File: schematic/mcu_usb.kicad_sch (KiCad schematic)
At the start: 40 parts, among them J2 USB4105-xx-A, J3 TC2030-IDC-NL, U1 STM32H563ZIT6, U4 USBLC6-2SC6, U5 TMP1075D, Y1 25MHz ABM8G

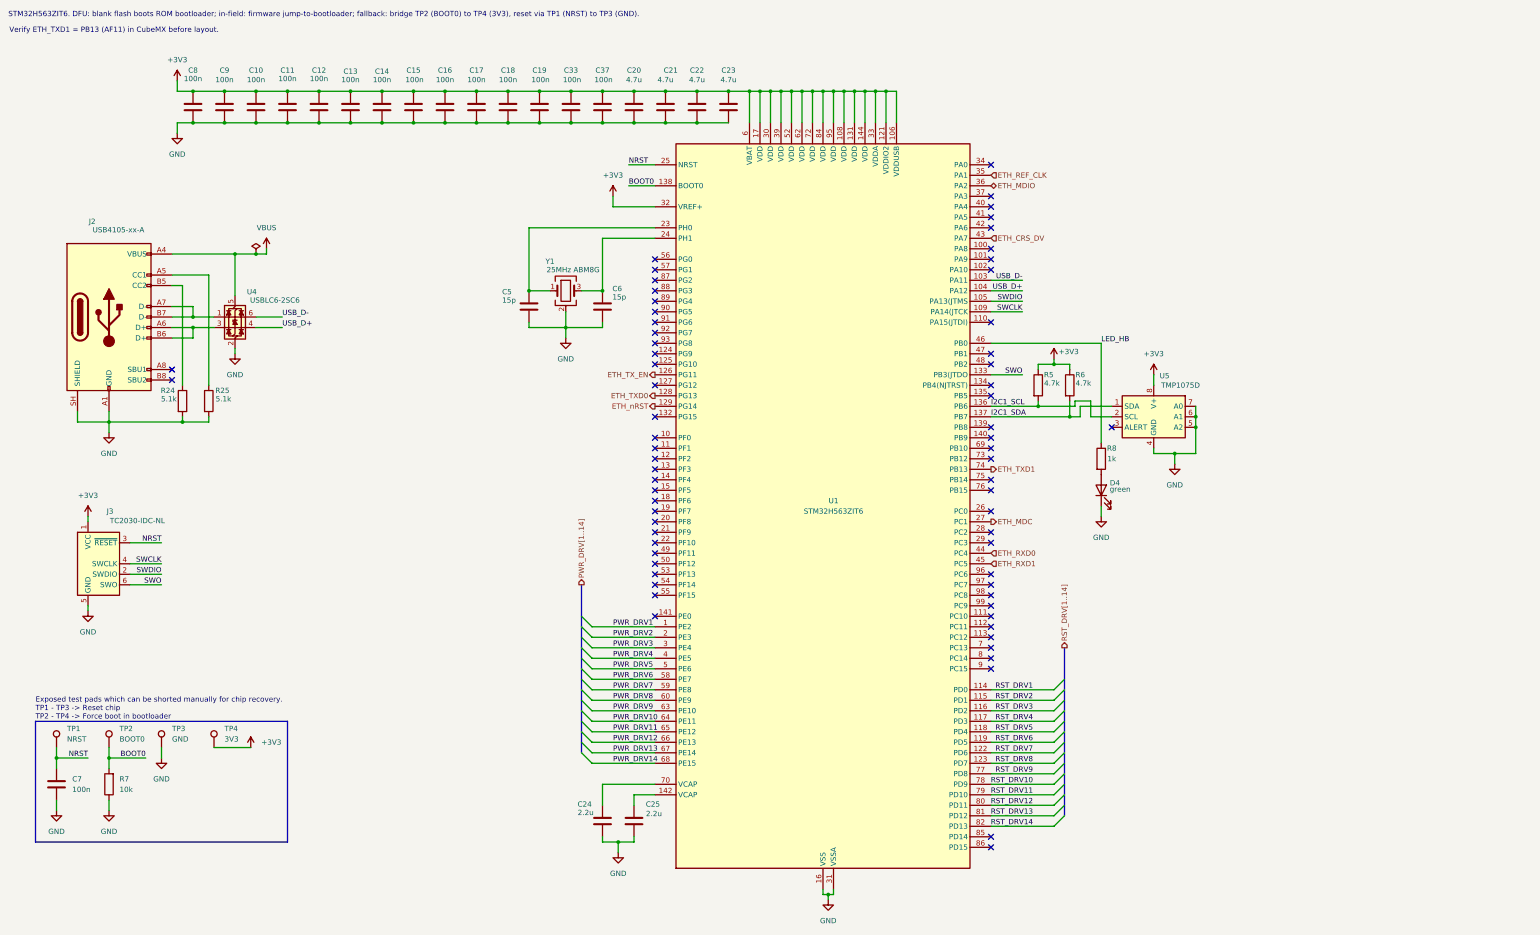
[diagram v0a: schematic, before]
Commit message: Swap to smaller MCU package with less pins
Signed-off-by: Lee Smet <lee.smet@hotmail.com>
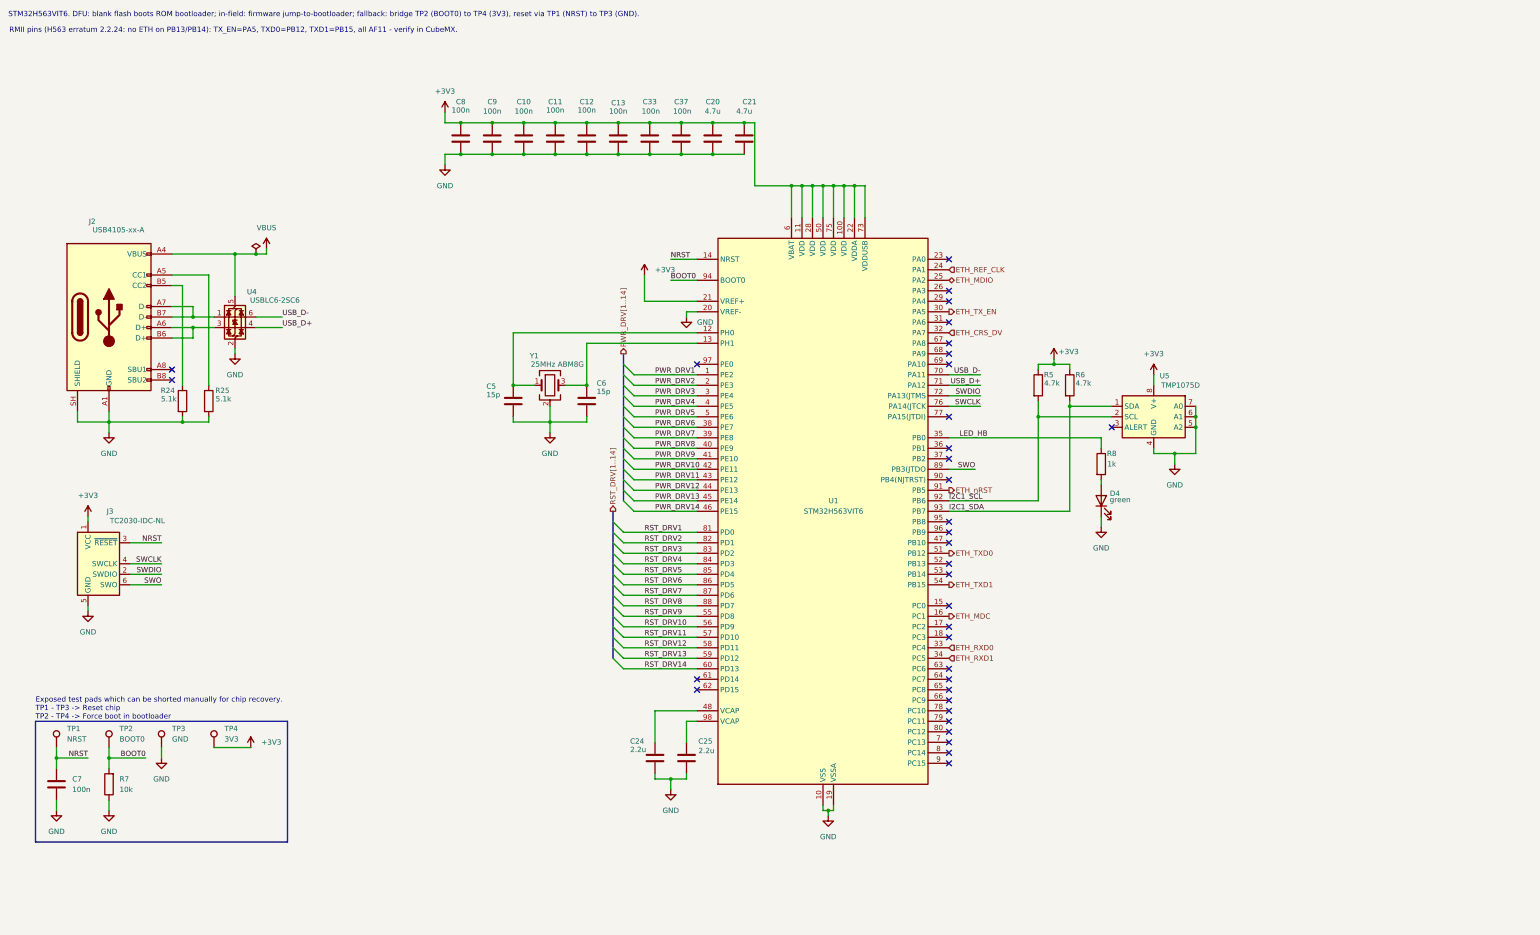
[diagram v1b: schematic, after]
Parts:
- removed C14, C15, C16, C17, C18, C19: 100n, Capacitor_SMD:C_0402_1005Metric, symbol Device:C
- removed C22, C23: 4.7u, Capacitor_SMD:C_0603_1608Metric, symbol Device:C
- U1: value STM32H563ZIT6 -> STM32H563VIT6; footprint Package_QFP:LQFP-144_20x20mm_P0.5mm -> Package_QFP:LQFP-100_14x14mm_P0.5mm; symbol MCU_ST_STM32H5:STM32H563ZITx -> MCU_ST_STM32H5:STM32H563VITx
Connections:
- net +3V3: now also U1.100 (VDD), U1.11 (VDD), U1.21 (VREF+), U1.22 (VDDA), U1.28 (VDD), U1.50 (VDD), U1.73 (VDDUSB), U1.75 (VDD); no longer U1.106 (VDDUSB), U1.108 (VDD), U1.121 (VDDIO2), U1.131 (VDD), U1.144 (VDD), U1.17 (VDD), U1.30 (VDD), U1.32 (VREF+), U1.33 (VDDA), U1.39 (VDD), U1.52 (VDD), U1.62 (VDD), U1.72 (VDD), U1.84 (VDD), U1.95 (VDD)
- net BOOT0: now also U1.94 (BOOT0); no longer U1.138 (BOOT0)
- net ETH_CRS_DV: now also U1.32 (PA7); no longer U1.43 (PA7)
- net ETH_MDC: now also U1.16 (PC1); no longer U1.27 (PC1)
- net ETH_MDIO: now also U1.25 (PA2); no longer U1.36 (PA2)
- net ETH_REF_CLK: now also U1.24 (PA1); no longer U1.35 (PA1)
- net ETH_RXD0: now also U1.33 (PC4); no longer U1.44 (PC4)
- net ETH_RXD1: now also U1.34 (PC5); no longer U1.45 (PC5)
- net ETH_TXD0: now also U1.51 (PB12); no longer U1.128 (PG13)
- net ETH_TXD1: now also U1.54 (PB15); no longer U1.74 (PB13)
- net ETH_TX_EN: now also U1.30 (PA5); no longer U1.126 (PG11)
- net ETH_nRST: now also U1.91 (PB5); no longer U1.129 (PG14)
- net GND: now also U1.10 (VSS), U1.19 (VSSA), U1.20 (VREF-), U1.27 (VSS), U1.49 (VSS), U1.74 (VSS), U1.99 (VSS); no longer U1.107 (VSS), U1.120 (VSS), U1.130 (VSS), U1.143 (VSS), U1.16 (VSS), U1.31 (VSSA), U1.38 (VSS), U1.51 (VSS), U1.61 (VSS), U1.71 (VSS), U1.83 (VSS), U1.94 (VSS)
- net I2C1_SCL: now also U1.92 (PB6); no longer U1.136 (PB6)
- net I2C1_SDA: now also U1.93 (PB7); no longer U1.137 (PB7)
- net LED_HB: now also U1.35 (PB0); no longer U1.46 (PB0)
- net NRST: now also U1.14 (NRST); no longer U1.25 (NRST)
- net PWR_DRV10: now also U1.42 (PE11); no longer U1.64 (PE11)
- net PWR_DRV11: now also U1.43 (PE12); no longer U1.65 (PE12)
- net PWR_DRV12: now also U1.44 (PE13); no longer U1.66 (PE13)
- net PWR_DRV13: now also U1.45 (PE14); no longer U1.67 (PE14)
- net PWR_DRV14: now also U1.46 (PE15); no longer U1.68 (PE15)
- net PWR_DRV6: now also U1.38 (PE7); no longer U1.58 (PE7)
- net PWR_DRV7: now also U1.39 (PE8); no longer U1.59 (PE8)
- net PWR_DRV8: now also U1.40 (PE9); no longer U1.60 (PE9)
- net PWR_DRV9: now also U1.41 (PE10); no longer U1.63 (PE10)
- net RST_DRV1: now also U1.81 (PD0); no longer U1.114 (PD0)
- net RST_DRV10: now also U1.56 (PD9); no longer U1.78 (PD9)
- net RST_DRV11: now also U1.57 (PD10); no longer U1.79 (PD10)
- net RST_DRV12: now also U1.58 (PD11); no longer U1.80 (PD11)
- net RST_DRV13: now also U1.59 (PD12); no longer U1.81 (PD12)
- net RST_DRV14: now also U1.60 (PD13); no longer U1.82 (PD13)
- net RST_DRV2: now also U1.82 (PD1); no longer U1.115 (PD1)
- net RST_DRV3: now also U1.83 (PD2); no longer U1.116 (PD2)
- net RST_DRV4: now also U1.84 (PD3); no longer U1.117 (PD3)
- net RST_DRV5: now also U1.85 (PD4); no longer U1.118 (PD4)
- net RST_DRV6: now also U1.86 (PD5); no longer U1.119 (PD5)
- net RST_DRV7: now also U1.87 (PD6); no longer U1.122 (PD6)
- net RST_DRV8: now also U1.88 (PD7); no longer U1.123 (PD7)
- net RST_DRV9: now also U1.55 (PD8); no longer U1.77 (PD8)
- net SWCLK: now also U1.76 (PA14(JTCK); no longer U1.109 (PA14(JTCK)
- net SWDIO: now also U1.72 (PA13(JTMS); no longer U1.105 (PA13(JTMS)
- net SWO: now also U1.89 (PB3(JTDO); no longer U1.133 (PB3(JTDO)
- net USB_D+: now also U1.71 (PA12); no longer U1.104 (PA12)
- net USB_D-: now also U1.70 (PA11); no longer U1.103 (PA11)
- net at C6.1, Y1.3: now also U1.13 (PH1); no longer U1.24 (PH1)
- net at U1.12 (PH0): now also C5.1, Y1.1
- net at C25.1: now also U1.98 (VCAP); no longer U1.142 (VCAP)
- net at U1.48 (VCAP): now also C24.1
- now unconnected: U1.23 (PH0)
- no-connect marks 67 -> 35
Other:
- note added: "RMII pins (H563 erratum 2.2.24: no ETH on PB13/PB14): TX_EN=PA5, TXD0=PB12, TXD1=PB15, all AF11 - verify in CubeMX."
- note added: "STM32H563VIT6. DFU: blank flash boots ROM bootloader; in-field: firmware jump-to-bootloader; fallback: bridge TP2 (BOOT0) to TP4 (3V3), reset via TP1 (NRST) to TP3 (GND)."
- note removed: "STM32H563ZIT6. DFU: blank flash boots ROM bootloader; in-field: firmware jump-to-bootloader; fallback: bridge TP2 (BOOT0) to TP4 (3V3), reset via TP1 (NRST) to TP3 (GND)."
- note removed: "Verify ETH_TXD1 = PB13 (AF11) in CubeMX before layout."
- moved on the sheet: C10, C11, C12, C13, C20, C21, C24, C25, C33, C37, C5, C6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

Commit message: More schematic works
Signed-off-by: Lee Smet <lee.smet@hotmail.com>
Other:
- note added: "One 100nF cap per supply pin Bulk caps: 1 on power trace entry in MCU area, 1 on other side of MCU, relaxed"
- moved on the sheet: C10, C11, C12, C13, C20, C21, C33, C37, C8, C9

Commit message: Add manufacturer and MPN to schematic parts
Signed-off-by: Lee Smet <lee.smet@hotmail.com>
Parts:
- C10, C11, C12, C13, C33, C37, C7, C8, C9: MANUFACTURER (none) -> YAGEO; MPN (none) -> CC0402KRX7R7BB104
- C20, C21: MANUFACTURER (none) -> Samsung Electro-Mechanics; MPN (none) -> CL10A475KO8NNNC
- C24, C25: MANUFACTURER (none) -> Samsung Electro-Mechanics; MPN (none) -> CL10A225KA8NNNC
- C5, C6: MANUFACTURER (none) -> Murata; MPN (none) -> GRM1555C1H150JA01D
- D4: MANUFACTURER (none) -> Kingbright; MPN (none) -> APT1608LZGCK
- J2: MANUFACTURER (none) -> Global Connector Technology; MPN (none) -> USB4105-GF-A
- J3: MANUFACTURER (none) -> Tag-Connect; MPN (none) -> TC2030-IDC-NL
- R24, R25: MANUFACTURER (none) -> YAGEO; MPN (none) -> RC0402FR-075K1L
- R5, R6: MANUFACTURER (none) -> YAGEO; MPN (none) -> RC0402FR-074K7L
- R7: MANUFACTURER (none) -> UNI-ROYAL; MPN (none) -> 0402WGF1002TCE
- R8: MANUFACTURER (none) -> YAGEO; MPN (none) -> RC0402FR-071KL
- U1: MANUFACTURER (none) -> STMicroelectronics; MPN (none) -> STM32H563VIT6
- U4: MANUFACTURER (none) -> STMicroelectronics; MPN (none) -> USBLC6-2SC6
- U5: MANUFACTURER (none) -> Texas Instruments; MPN (none) -> TMP1075DR
- Y1: MANUFACTURER (none) -> Abracon; MPN (none) -> ABM8G-25.000MHZ-B4Y-T3

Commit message: Finish adding external temp probes
Signed-off-by: Lee Smet <lee.smet@hotmail.com>
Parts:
- added D5: ESD9L5.0ST5G, Diode_SMD:D_SOD-923, symbol Device:D_Zener
- added J4, J5, J6, J7: 1WIRE, Connector_JST:JST_PH_B3B-PH-K_1x03_P2.00mm_Vertical, symbol Connector_Generic:Conn_01x03
- added R30: 4.7k, Resistor_SMD:R_0402_1005Metric, symbol Device:R
- added R31: 100, Resistor_SMD:R_0603_1608Metric, symbol Device:R
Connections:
- net +3V3: now also J4.1 (Pin_1), J5.1 (Pin_1), J6.1 (Pin_1), J7.1 (Pin_1), R30.1
- net GND: now also D5.2 (A), J4.3 (Pin_3), J5.3 (Pin_3), J6.3 (Pin_3), J7.3 (Pin_3)
- net OW_MCU: now reaches U1.68 (PA9)
- net OW_MCU: now also R31.1
- new net OW_DATA: D5.1 (K), J4.2 (Pin_2), J5.2 (Pin_2), J6.2 (Pin_2), J7.2 (Pin_2), R30.2, R31.2
- no-connect marks 35 -> 34
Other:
- note added: "External Temperature Probe Connectors Connect to DS18B20 temperature probes"

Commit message: Exclude test pads and Tag-Connect land from BOM
TP1-TP4 and J3 are bare copper with nothing to place; keep them out
of the assembly BOM. Footprint attributes updated to match.
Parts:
- J3, TP1, TP2, TP3, TP4: now left out of the parts list

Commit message: Add protected GPIO expansion header
New sheet 'Expansion header' with J8, a 2x18 2.54 mm header (DNP),
bringing out the 28 spare U1 GPIOs plus I2C1, 3V3 and 5V.

- Each signal: 330R series resistor (4x0402 array, MCU side) and a
  TPD4E05U06 ESD clamp at the header pin.
- 3V3 and 5V header pins: PTC fuse plus a TVS to GND.
- PC13-PC15 stay unconnected (backup domain, LSE).
- U1 spare pins labelled GPIO_<pin>; the I2C1 labels on U1 became
  global so the header can reach the bus. Net class patterns added
  for I2C1_*, HDR_3V3 and HDR_5V.
- Board regenerated from the netlist (nothing was placed yet).
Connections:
- net GPIO_PC0: now reaches U1.15 (PC0)
- net GPIO_PC2: now reaches U1.17 (PC2)
- net GPIO_PC3: now reaches U1.18 (PC3)
- net GPIO_PA0: now reaches U1.23 (PA0)
- net GPIO_PA3: now reaches U1.26 (PA3)
- net GPIO_PA4: now reaches U1.29 (PA4)
- net GPIO_PA6: now reaches U1.31 (PA6)
- net GPIO_PB1: now reaches U1.36 (PB1)
- net GPIO_PB2: now reaches U1.37 (PB2)
- net GPIO_PB10: now reaches U1.47 (PB10)
- net GPIO_PB13: now reaches U1.52 (PB13)
- net GPIO_PB14: now reaches U1.53 (PB14)
- net GPIO_PD14: now reaches U1.61 (PD14)
- net GPIO_PD15: now reaches U1.62 (PD15)
- net GPIO_PC6: now reaches U1.63 (PC6)
- net GPIO_PC7: now reaches U1.64 (PC7)
- net GPIO_PC8: now reaches U1.65 (PC8)
- net GPIO_PC9: now reaches U1.66 (PC9)
- net GPIO_PA8: now reaches U1.67 (PA8)
- net GPIO_PA10: now reaches U1.69 (PA10)
- net GPIO_PA15: now reaches U1.77 (PA15(JTDI))
- net GPIO_PC10: now reaches U1.78 (PC10)
- net GPIO_PC11: now reaches U1.79 (PC11)
- net GPIO_PC12: now reaches U1.80 (PC12)
- net GPIO_PB4: now reaches U1.90 (PB4(NJTRST))
- net GPIO_PB8: now reaches U1.95 (PB8)
- net GPIO_PB9: now reaches U1.96 (PB9)
- net GPIO_PE0: now reaches U1.97 (PE0)
- no-connect marks 34 -> 6

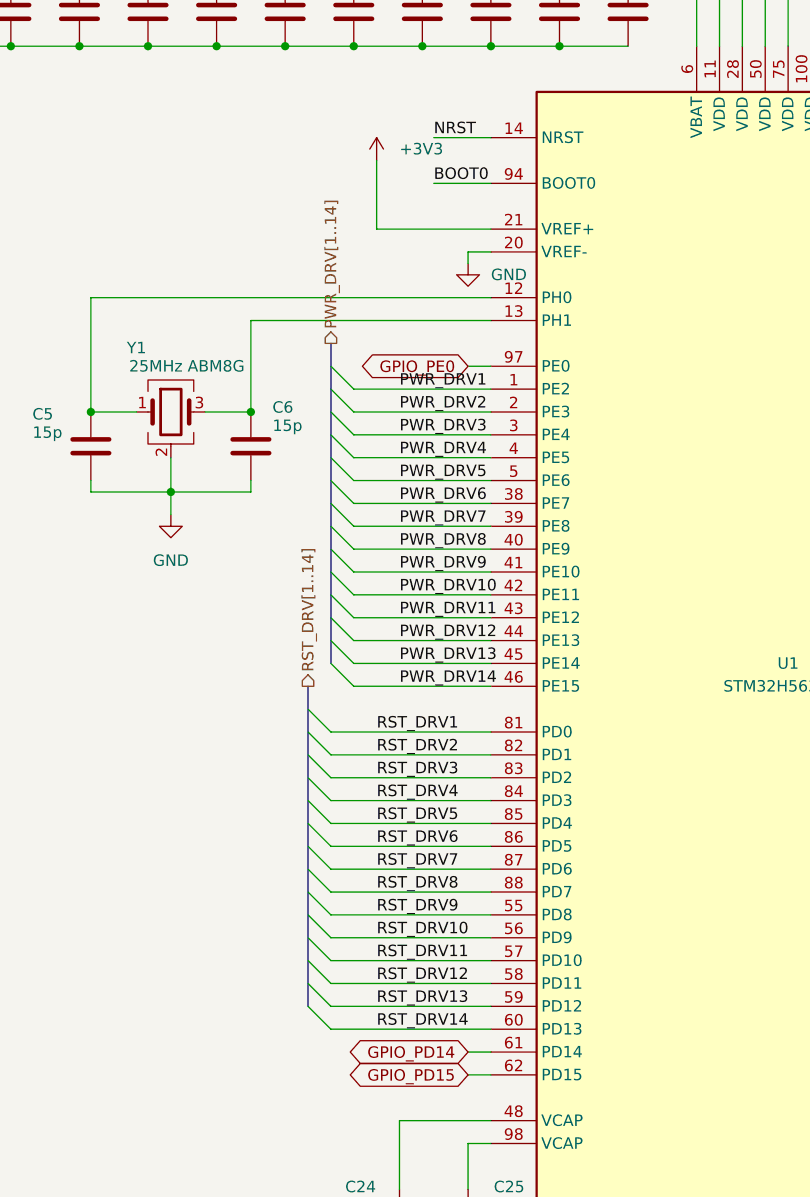
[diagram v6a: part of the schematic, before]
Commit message: Rework for 8 nodes with MCP23017 relay drive
Target is now 8 motherboards per frame (was 14 in the schematic).

- relays_a/relays_b (14 channels, 28 photoMOS) replaced by one
  'Relay channels' sheet: 8 channels, 16 TLP176AM, J11-J18, same
  per-channel circuit and parts.
- U14 MCP23017 @0x20 drives the LEDs: GPA0-7 = PWR_DRV1-8,
  GPB0-7 = RST_DRV1-8. R32 pulls EXP_nRESET low so U14 stays in
  reset (all buttons released) unless the MCU drives it; R33 pulls
  up the shared open-drain EXP_INT.
- MCU: the two 14-bit drive buses are gone; PE2 = EXP_nRESET,
  PE3 = EXP_INT, the other 26 freed pins are no-connect.
- Expansion header J8 grows to 2x20 and carries I2C1, EXP_nRESET
  and EXP_INT (pins 5-8) for extra expander modules or a later
  power board, plus 3V3/5V on both ends.
- Net classes for the second relay bank removed; drive patterns
  point at the new sheet. Board regenerated (nothing placed).
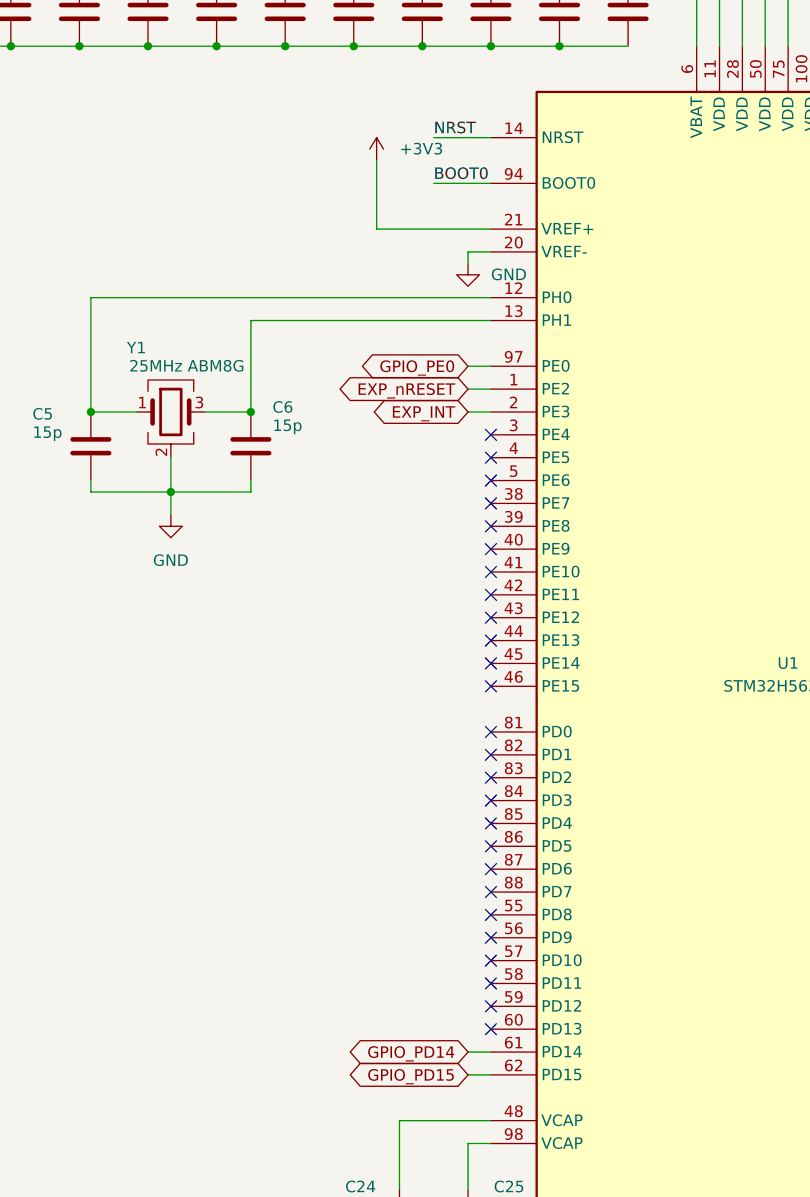
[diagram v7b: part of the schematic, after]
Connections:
- net PWR_DRV1 renamed EXP_nRESET
- net PWR_DRV10: no longer names the net of U1.42 (PE11)
- net PWR_DRV11: no longer names the net of U1.43 (PE12)
- net PWR_DRV12: no longer names the net of U1.44 (PE13)
- net PWR_DRV13: no longer names the net of U1.45 (PE14)
- net PWR_DRV14: no longer names the net of U1.46 (PE15)
- net PWR_DRV2 renamed EXP_INT
- net PWR_DRV3: no longer names the net of U1.3 (PE4)
- net PWR_DRV4: no longer names the net of U1.4 (PE5)
- net PWR_DRV5: no longer names the net of U1.5 (PE6)
- net PWR_DRV6: no longer names the net of U1.38 (PE7)
- net PWR_DRV7: no longer names the net of U1.39 (PE8)
- net PWR_DRV8: no longer names the net of U1.40 (PE9)
- net PWR_DRV9: no longer names the net of U1.41 (PE10)
- net RST_DRV1: no longer names the net of U1.81 (PD0)
- net RST_DRV10: no longer names the net of U1.56 (PD9)
- net RST_DRV11: no longer names the net of U1.57 (PD10)
- net RST_DRV12: no longer names the net of U1.58 (PD11)
- net RST_DRV13: no longer names the net of U1.59 (PD12)
- net RST_DRV14: no longer names the net of U1.60 (PD13)
- net RST_DRV2: no longer names the net of U1.82 (PD1)
- net RST_DRV3: no longer names the net of U1.83 (PD2)
- net RST_DRV4: no longer names the net of U1.84 (PD3)
- net RST_DRV5: no longer names the net of U1.85 (PD4)
- net RST_DRV6: no longer names the net of U1.86 (PD5)
- net RST_DRV7: no longer names the net of U1.87 (PD6)
- net RST_DRV8: no longer names the net of U1.88 (PD7)
- net RST_DRV9: no longer names the net of U1.55 (PD8)
- no-connect marks 6 -> 32
